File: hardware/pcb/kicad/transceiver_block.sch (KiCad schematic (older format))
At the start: 22 parts, among them CON2 RJ45_TART, CON3 RJ45_TART, IC2 LTC2851, IC3 LTC2851, IC4 LTC2851, IC5 LTC2851, IC6 LTC2851, IC7 LTC2851

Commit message: Updated silkscreen ready for manufacture
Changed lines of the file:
@@
 Sheet 4 7
 Title ""
-Date "29 oct 2014"
+Date "30 oct 2014"
 Rev ""
 Comp ""
@@
 P 2950 6250
 AR Path="/5409247B/54067578" Ref="IC7"  Part="1"
-AR Path="/540924B7/54067578" Ref="IC2"  Part="1"
+AR Path="/540924B7/54067578" Ref="IC13"  Part="1"
 AR Path="/54092498/54067578" Ref="IC19"  Part="1"
 AR Path="/540670D5/54067578" Ref="IC25"  Part="1"
-F 0 "IC2" H 2950 6150 50  0000 C CNN
+F 0 "IC13" H 2950 6150 50  0000 C CNN
 F 1 "LTC2851" H 2950 6350 50  0000 C CNN
 F 2 "MODULE" H 2950 6250 50  0001 C CNN
@@
 P 2950 5350
 AR Path="/5409247B/54067576" Ref="IC6"  Part="1"
-AR Path="/540924B7/54067576" Ref="IC3"  Part="1"
+AR Path="/540924B7/54067576" Ref="IC12"  Part="1"
 AR Path="/54092498/54067576" Ref="IC18"  Part="1"
 AR Path="/540670D5/54067576" Ref="IC24"  Part="1"
-F 0 "IC3" H 2950 5250 50  0000 C CNN
+F 0 "IC12" H 2950 5250 50  0000 C CNN
 F 1 "LTC2851" H 2950 5450 50  0000 C CNN
 F 2 "MODULE" H 2950 5350 50  0001 C CNN
@@
 P 2950 4450
 AR Path="/5409247B/54067575" Ref="IC5"  Part="1"
-AR Path="/540924B7/54067575" Ref="IC1"  Part="1"
+AR Path="/540924B7/54067575" Ref="IC11"  Part="1"
 AR Path="/54092498/54067575" Ref="IC17"  Part="1"
 AR Path="/540670D5/54067575" Ref="IC23"  Part="1"
-F 0 "IC1" H 2950 4350 50  0000 C CNN
+F 0 "IC11" H 2950 4350 50  0000 C CNN
 F 1 "LTC2851" H 2950 4550 50  0000 C CNN
 F 2 "MODULE" H 2950 4450 50  0001 C CNN
@@
 P 2950 3550
 AR Path="/5409247B/54067570" Ref="IC4"  Part="1"
-AR Path="/540924B7/54067570" Ref="IC5"  Part="1"
+AR Path="/540924B7/54067570" Ref="IC10"  Part="1"
 AR Path="/54092498/54067570" Ref="IC16"  Part="1"
 AR Path="/540670D5/54067570" Ref="IC22"  Part="1"
-F 0 "IC5" H 2950 3450 50  0000 C CNN
+F 0 "IC10" H 2950 3450 50  0000 C CNN
 F 1 "LTC2851" H 2950 3650 50  0000 C CNN
 F 2 "MODULE" H 2950 3550 50  0001 C CNN
@@
 P 2950 2650
 AR Path="/5409247B/5406756F" Ref="IC3"  Part="1"
-AR Path="/540924B7/5406756F" Ref="IC6"  Part="1"
+AR Path="/540924B7/5406756F" Ref="IC9"  Part="1"
 AR Path="/54092498/5406756F" Ref="IC15"  Part="1"
 AR Path="/540670D5/5406756F" Ref="IC21"  Part="1"
-F 0 "IC6" H 2950 2550 50  0000 C CNN
+F 0 "IC9" H 2950 2550 50  0000 C CNN
 F 1 "LTC2851" H 2950 2750 50  0000 C CNN
 F 2 "MODULE" H 2950 2650 50  0001 C CNN
@@
 P 2950 1750
 AR Path="/5409247B/5406756E" Ref="IC2"  Part="1"
-AR Path="/540924B7/5406756E" Ref="IC4"  Part="1"
+AR Path="/540924B7/5406756E" Ref="IC8"  Part="1"
 AR Path="/54092498/5406756E" Ref="IC14"  Part="1"
 AR Path="/540670D5/5406756E" Ref="IC20"  Part="1"
-F 0 "IC4" H 2950 1650 50  0000 C CNN
+F 0 "IC8" H 2950 1650 50  0000 C CNN
 F 1 "LTC2851" H 2950 1850 50  0000 C CNN
 F 2 "MODULE" H 2950 1750 50  0001 C CNN

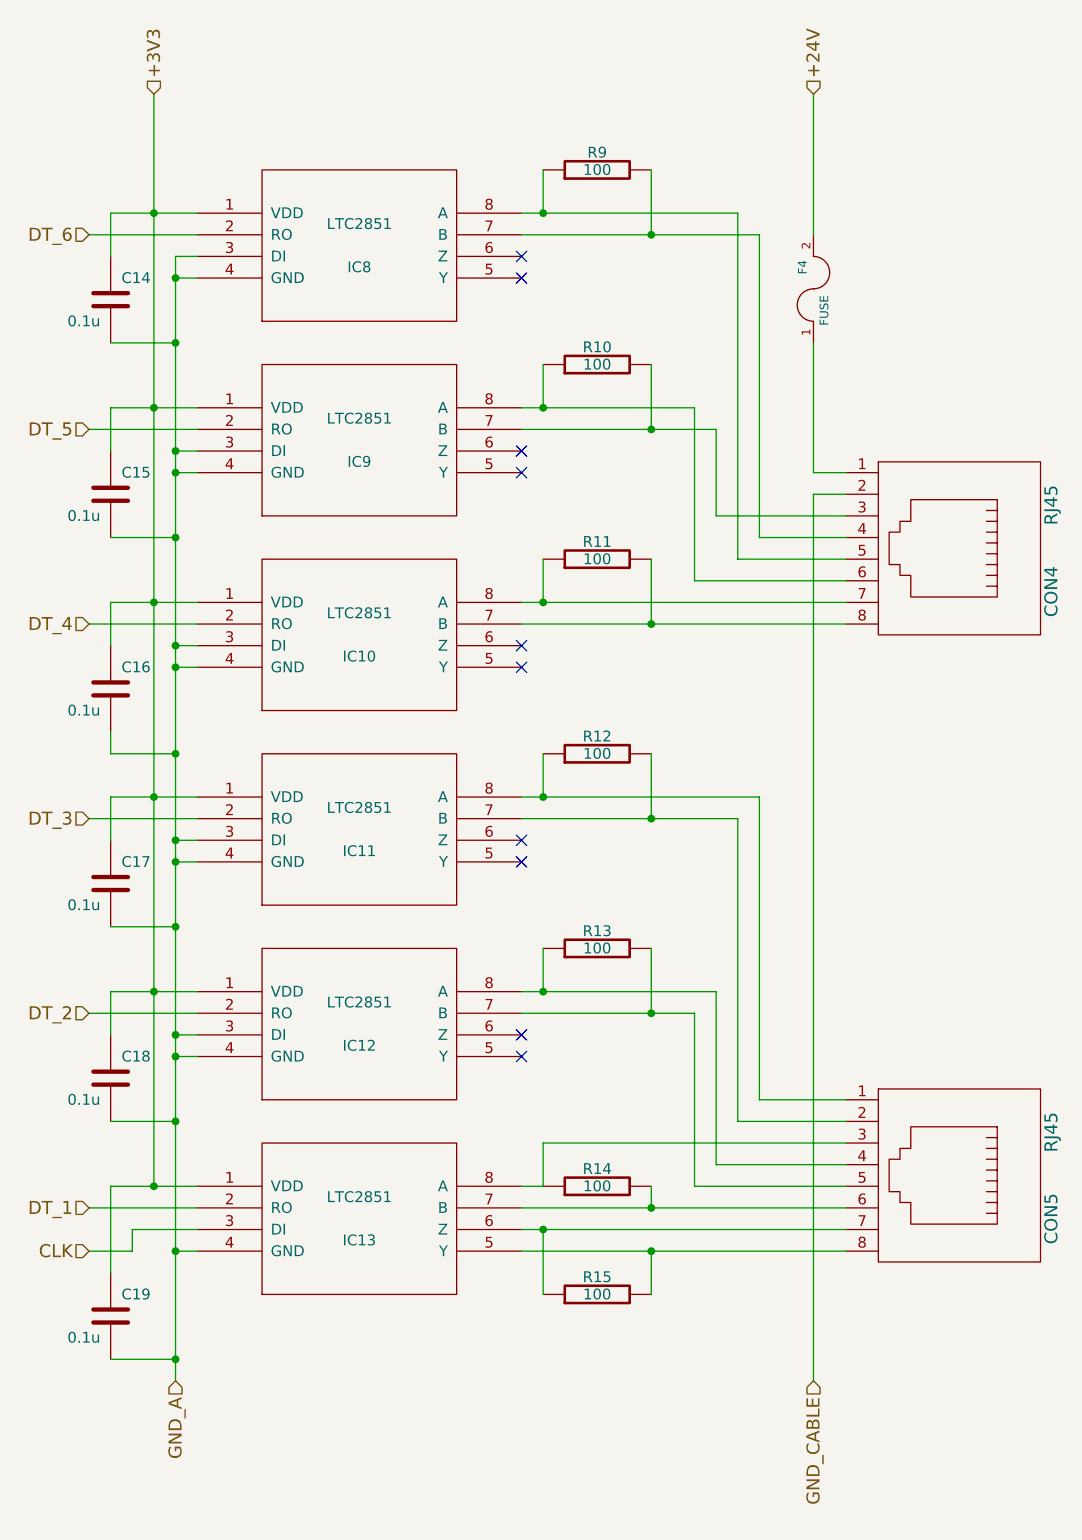
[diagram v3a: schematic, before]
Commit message: Made component references more logical - very similar to eagle version
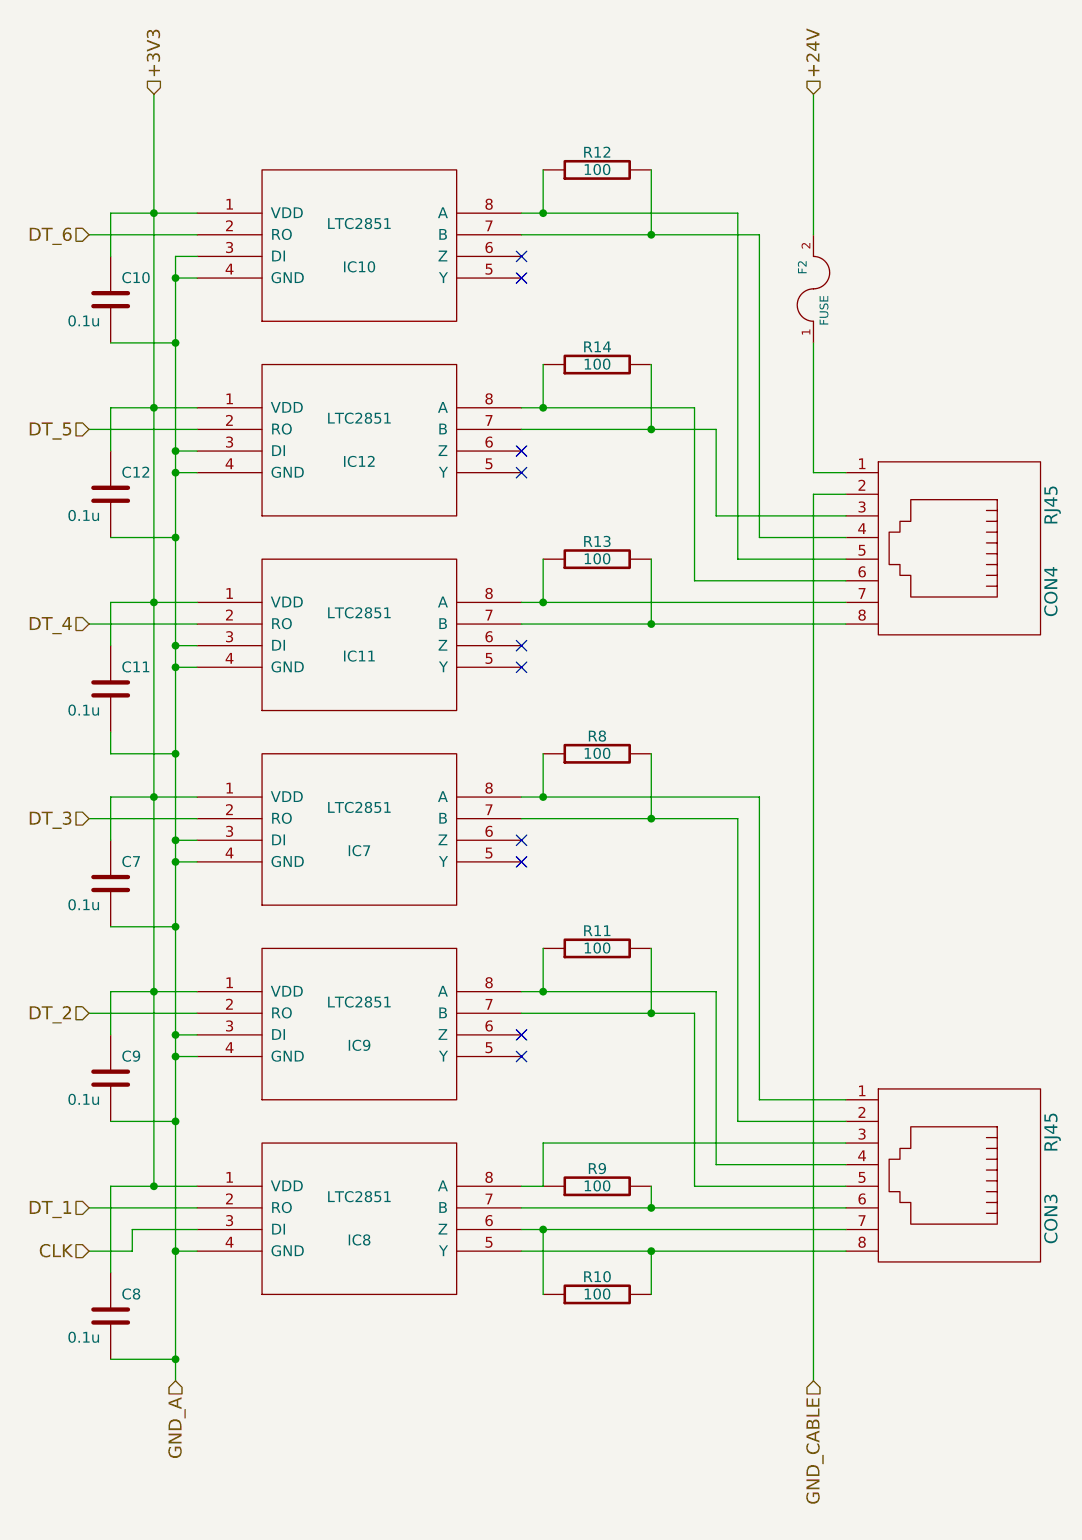
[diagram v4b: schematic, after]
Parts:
- renumbered C11 to C13, C13 to C14, C12 to C15, C8 to C16, C10 to C17, C9 to C18, CON3 to CON5, CON2 to CON6, F4 to F1, IC5 to IC13, IC7 to IC14, IC6 to IC15, IC2 to IC16, IC4 to IC17, IC3 to IC18, R5 to R15, R7 to R16, R8 to R17, R6 to R18, R2 to R19, R4 to R20, R3 to R21
